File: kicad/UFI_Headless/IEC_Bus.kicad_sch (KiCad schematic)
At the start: 8 parts, among them J8 IEC_HDR, U10 74LVC14AD, U9 SN74LS07D

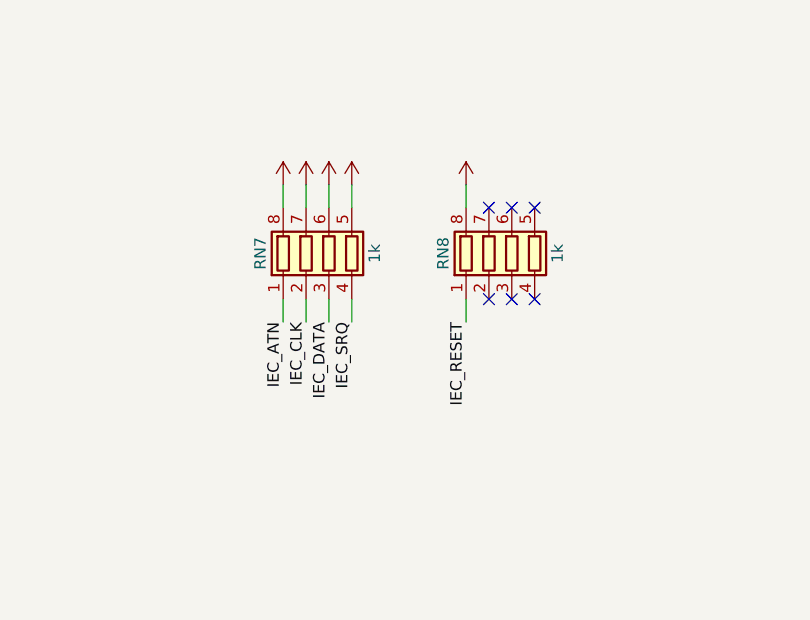
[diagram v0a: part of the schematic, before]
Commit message: KiCad v0.7 rework, schematic stages A1-A3: automatic 5 V source selection, discrete FDD termination, front-panel header - Power: J18 (5V_SEL jumper) removed, U19 TPS2116DRL selects external 5 V (J17, priority) or the 12 V buck automatically (R72 33k / R73 10k PR1 divider, C57 1 uF, status via R74 10k to +3V3 on test point TP9 TP_5V_SEL), PWR_FLAG moved to +5V_PSU_F; Flux_Interface / IEC_Bus / FDD_Connectors: RN1-RN8 (1k R_Pack04) replaced by 25 discrete 0603 1k resistors R75-R99 on the same nets (17 FDD lines, 5 IEC, 3 Amiga), array stubs, per-pin +5V symbols and orphan no-connects removed; MCU_Core: J9 EXPANSION and J13 MODE_SW removed, J12 becomes a keyed 2x8 IDC front-panel header FRONT (1 +3V3, 3 ACT, 5 ERR, 7 USB, 9 FDD, 11 PWR via R34-R37 and new R100 330 R, 13 BTN_A, 14 BTN_B, 15 MODE1, 16 MODE2 via R101-R104 470 R and TVS D18-D21, even pins 2-12 GND), on-board LEDs D5-D8 with R12-R15 removed (D4 ACT stays), SW3/SW4 marked DNP (buttons on the front); lib_symbols for Conn_02x08_Odd_Even and D_TVS added to MCU_Core; ERC over the whole project 0 errors / 0 warnings. Design brief docs/PCB_Revision_Empfehlungen_2026-10-24.md (decisions of 2026-10-24: power as before minus J18, input edge vs. drive edge, DB23 Amiga at the drive edge, W5500 LAN at the input edge, 32x 0603 termination), bring-up procedure docs/Bringup_2026-10-24.md (USB-C J1 soldered rotated 180 deg on the first board). Open for A4/A5: INDEX_SIM needs its own timer-capable MCU pin (PE1 is now the MODE2 line; firmware pin map changes in the same commit as the schematic), I2C SCL/SDA get 4 test pads, D18-D21 to be swapped for low-leakage ESD diodes (SMF3.3CA leaks up to 1 mA at 3.3 V against ~40k internal pull-ups) plus ESD on the five LED lines, +3V3 on J12 pin 1 to be fed through a 1k series resistor, loopback block, LA header, J11 slide switch, DIN-6 and DB23, W5500, then layout (USB-C edge cutout, input/output edges). Layout (.kicad_pcb) not yet touched.
Claude-Session: https://claude.ai/code/sessi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
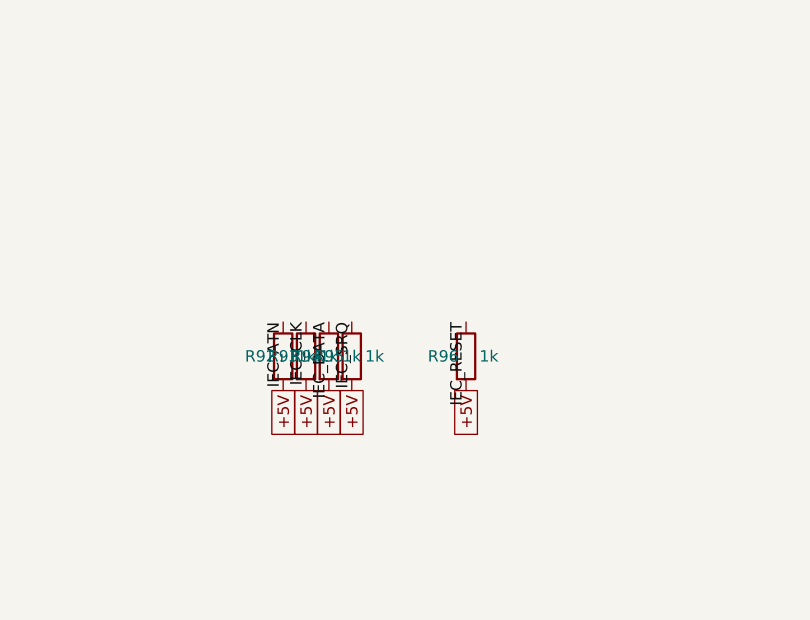
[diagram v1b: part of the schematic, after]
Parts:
- removed RN7, RN8: 1k, Resistor_SMD:R_Array_Convex_4x0603, symbol Device:R_Pack04
- added R92, R93, R94, R95, R96: 1k, Resistor_SMD:R_0603_1608Metric, symbol Device:R
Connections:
- net +5V: now also R92.2, R93.2, R94.2, R95.2, R96.2
- net IEC_ATN: now also R92.1
- net IEC_CLK: now also R93.1
- net IEC_DATA: now also R94.1
- net IEC_RESET: now also R96.1
- net IEC_SRQ: now also R95.1
- no-connect marks 8 -> 2

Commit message: KiCad v0.7 rework, schematic stage A4 with the matching firmware pin map: electronic self-test loopback, index simulation on its own timer pin, PSU-guard header, LA header - owner's constraint of 2026-10-24: the board sits in a closed enclosure, only LAN and USB stay reachable, nothing is pluggable after assembly, so no jumpers or slide switches for operation. Flux_Interface: J11 WRITE_LOCK pin header replaced by solder jumper JP4 (+3V3 to WLOCK, R33 100k pull-down and the U14 LVC1G32 hardware gate unchanged); INDEX_SIM is a global net from PE5 (TIM15_CH1, verified against the ST pin database via the embassy stm32h723zg tables) through the until now unused open-collector buffer U7F (pin 13 was tied to +5V) onto FD_INDEX, wired-OR like the J19 sync sensor, so the self-test index loop needs no wire; new loopback block U22 TS5A3166DBVR (SOT-23-5, pins 1 NO = FD_RDATA, 2 COM = FD_WDATA, 3 GND, 4 IN = LOOP_EN, 5 V+ = +5V; TI datasheet: V+ 1.65-5.5 V, VIH 2.4 V at 5 V, control input 0-5.5 V), C58 100n, R106 100k pull-down on LOOP_EN (open during reset), Q5 2N7002 pulls FD_TRK0 low with LOOP_EN; note text updated. IEC_Bus: the spare inverter U10F (input was GND, output no-connect) reads FD_WGATE back as WGATE_SENSE. MCU_Core: U5 PE5 INDEX_SIM, PG14 LOOP_EN, PG15 WGATE_SENSE, PG7 GUARD_OFF, PG8 GUARD_ERR5, PG13 GUARD_ERR12 (six no-connect flags removed); J20 GUARD 1x4 (1 GND, 2 OFF, 3 ERR5, 4 ERR12 with R107/R108 10k pull-ups) for the C64 PSU Guard board's J3; J21 LA 2x10 logic-analyser header on the 3.3 V side (1 RDATA, 3 WDATA, 5 INDEX, 7 WGATE, 9 STEP, 11 DIR, 13 SIDE, 15 DRVSEL_A, 17 MOTOR_A, 19 TRK0, 2 WPROT, 4 DSKCHG, 6 READY, 8 DENSITY, 10 INDEX_SIM, 12 LOOP_EN, 14 WGATE_SENSE, 16/18/20 GND); lib symbols TS5A3166DBVR, 2N7002, SolderJumper_2_Open, Conn_01x04, Conn_02x10_Odd_Even added to the sheets. ERC over the whole project 0 errors / 0 warnings. Firmware (same commit, as agreed): board.h/board_headless.c pin table PIN_INDEX_SIM PE5 (INDEX_SIM_AF = AF4), PIN_LOOP_EN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
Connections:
- net GND: no longer U10.13
- net WGATE_SENSE: now reaches U10.12
- new net FD_WGATE: U10.13
- no-connect marks 2 -> 1
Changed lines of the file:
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@@
-		)
-	)
-	(no_connect
-		(at 228.6 124.46)
-	)
-	(wire
-		(pts
-			(xy 213.36 124.46) (xy 210.82 124.46)
-		)
-		(stroke
-			(width 0)
-			(type default)
 		)
 	)
@@
 	)
 	(symbol
-		(lib_id "power:GND")
-		(at 210.82 124.46 270)
-		(unit 1)
-		(exclude_from_sim no)
-		(in_bom no)
-		(on_board yes)
-		(dnp no)
-		(property "Reference" "#PWR265"
-			(at 210.82 124.46 0)
-			(effects
-				(font
-					(size 1.27 1.27)
-				)
-				(hide yes)
-			)
-		)
-		(property "Value" "GND"
-			(at 210.82 124.46 0)
-			(effects
-				(font
-					(size 1.27 1.27)
-				)
-				(hide yes)
-			)
-		)
-		(property "Footprint" ""
-			(at 210.82 124.46 0)
-			(effects
-				(font
-					(size 1.27 1.27)
-				)
-				(hide yes)
-			)
-		)
-		(property "Datasheet" ""
-			(at 210.82 124.46 0)
-			(effects
-				(font
-					(size 1.27 1.27)
-				)
-				(hide yes)
-			)
-		)
-		(pin "1"
-		)
-		(instances
-			(project "UFI_Headless"
-				(path "/dc1b800d-cedf-5627-97f0-e6992ff33669/ed0b61ff-f6bd-56db-b8a4-25dbfb310cbc"
-					(reference "#PWR265")
-					(unit 1)
-				)
-			)
-		)
-	)
-	(symbol
 		(lib_id "74xx:74HC14")
 		(at 220.98 124.46 0)
@@
 		(effects
 			(font
+				(size 1.27 1.27)
+			)
+			(justify right)
+		)
+	)
+	(global_label "WGATE_SENSE"
+		(at 228.6 124.46 0)
+		(effects
+			(font
+				(size 1.27 1.27)
+			)
+			(justify left)
+		)
+	)
+	(global_label "FD_WGATE"
+		(at 213.35999999999999 124.46 180)
+		(effects
+			(font

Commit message: KiCad v0.7 rework, stage C part 1 (BOM completion before the release, review note H12): every BOM row now carries an LCSC number, checked against the JLCPCB SMT catalogue on 2026-10-25 (stock in brackets). LAN sheet: U23 W5500 C32843 (9019), J22 HR911105A C12074 (72229, THT), Y2 25 MHz 12 pF +-10 ppm YXC X322525MOB4SI C9006 (basic; load capacitance 12 pF verified on the LCSC parameter page, fits the 18 pF C59/C60), C59/C60 18 pF C0G Yageo CC0603JRNPO9BN180 C107040, C61/C74 10 nF FH 0603B103K500NT C57112 (basic), C71 22 nF Samsung CL10B223KB8NNNC C21122 (basic), C72/C73 6.8 nF FH 0603B682K500NT C1631 (basic), C62 4.7 uF C1779, C63/C69 10 uF C15850, C64-C68/C70 100 nF C14663, FB2 C1002, R109 1M C22935, R111 12.4k 1 % C22865, R112/R113 49.9R 1 % C23185 (basic), R114 10R 1 % C22859 (basic), R115/R116 82R 1 % C23255, R117/R118 330R C23138, R119-R124 10k C25804. Other sheets: R75-R99/R105/R128 1k C21190, R74/R107/R108 10k C25804, R101-R104/R130 470R C23179, R106/R131 100k C25803, C58 100 nF C14663 (value text 100n -> 100nF so it groups with the other 100 nF), D18-D26/D28/D29 PESD3V3L1BA C51450 (48710) like D32-D34, Q5 2N7002 C8545 (basic), U22 TS5A3166DBVR C353035 (10678), J2 DC-005 2.0 C16214 (92305; same pin pattern as the KiCad BarrelJack_Horizontal footprint, placement to be checked in the JLC viewer), J7 2x12 IDC ZHOURI DC3-2.54-24PAS C5144580 (stock 81 - hand soldering stays the recommendation in docs/Bestellung_JLC.md), J12 2x8 IDC DC3-2.54-16PAS C2977594 (4335), J16 2x5 pin header XFCN PZ254V-12-10P C492422 (105667), J21 2x10 pin header PZ254V-12-20P C492427 (63622). Solder jumpers JP5-JP8 are excluded from the BOM (in_bom no) like JP1/JP3 - bare copper, nothing to place. Stock of the review's watch list: U9 SN74LS07DR C371970 4776, D31 ESDA6V1-5SC6 C6650 3010, L1 SRN6045TA-150M C1330797 1866. BOM export (kicad-cli sch export bom, grouped by value/footprint/LCSC): 99 rows, 0 without LCSC, 0 DNP. ERC over the whole project 0 errors / 0 warnings (build/erc.rpt). No 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
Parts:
- R92, R93, R94, R95, R96: LCSC (none) -> C21190
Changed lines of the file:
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@@
+			)
+		)
+		(property "LCSC" "C21190"
+			(at 71.882 171.45 90)
+			(effects
+				(font
+					(size 1.27 1.27)
+				)
+				(hide yes)
 			)
 		)
@@
 			)
 		)
+		(property "LCSC" "C21190"
+			(at 74.422 171.45 90)
+			(effects
+				(font
+					(size 1.27 1.27)
+				)
+				(hide yes)
+			)
+		)
 		(property "Footprint" "Resistor_SMD:R_0603_1608Metric"
 			(at 74.422 171.45 90)
@@
 			)
 		)
+		(property "LCSC" "C21190"
+			(at 76.962 171.45 90)
+			(effects
+				(font
+					(size 1.27 1.27)
+				)
+				(hide yes)
+			)
+		)
 		(property "Footprint" "Resistor_SMD:R_0603_1608Metric"
 			(at 76.962 171.45 90)
@@
 			)
 		)
+		(property "LCSC" "C21190"
+			(at 79.502 171.45 90)
+			(effects
+				(font
+					(size 1.27 1.27)
+				)
+				(hide yes)
+			)
+		)
 		(property "Footprint" "Resistor_SMD:R_0603_1608Metric"
 			(at 79.502 171.45 90)
@@
 			)
 		)
+		(property "LCSC" "C21190"
+			(at 92.202 171.45 90)
+			(effects
+				(font
+					(size 1.27 1.27)
+				)
+				(hide yes)
+			)
+		)
